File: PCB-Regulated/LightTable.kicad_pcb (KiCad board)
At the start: 2 copper layers, 22 parts, among them CON1 BARREL_JACK, P1 CONN_2_V, P2 CONN_01X01, P3 CONN_01X01, P4 CONN_01X01, P5 CONN_01X01, P6 CONN_01X01, P7 CONN_01X01, P8 CONN_4_V, U1 MosfetIRF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

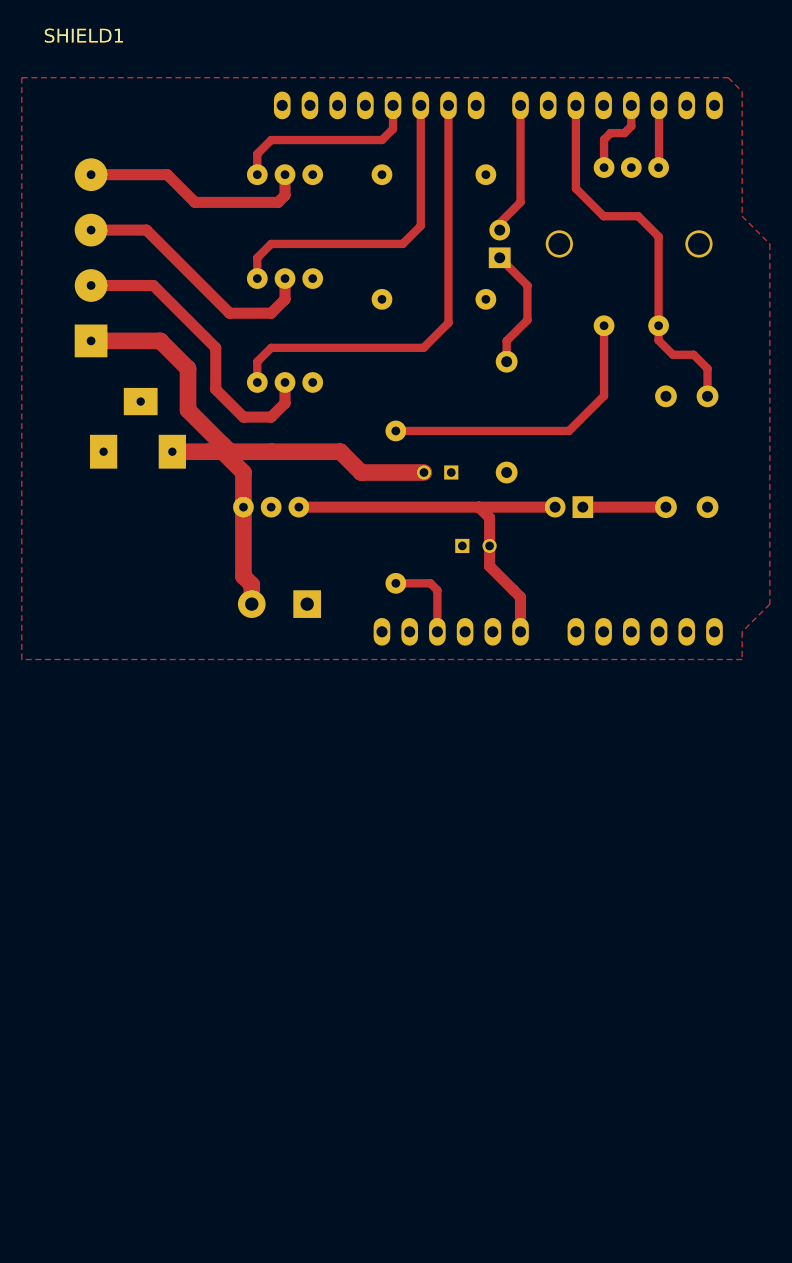
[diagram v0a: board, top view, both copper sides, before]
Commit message: Fixed wrong placement of shield
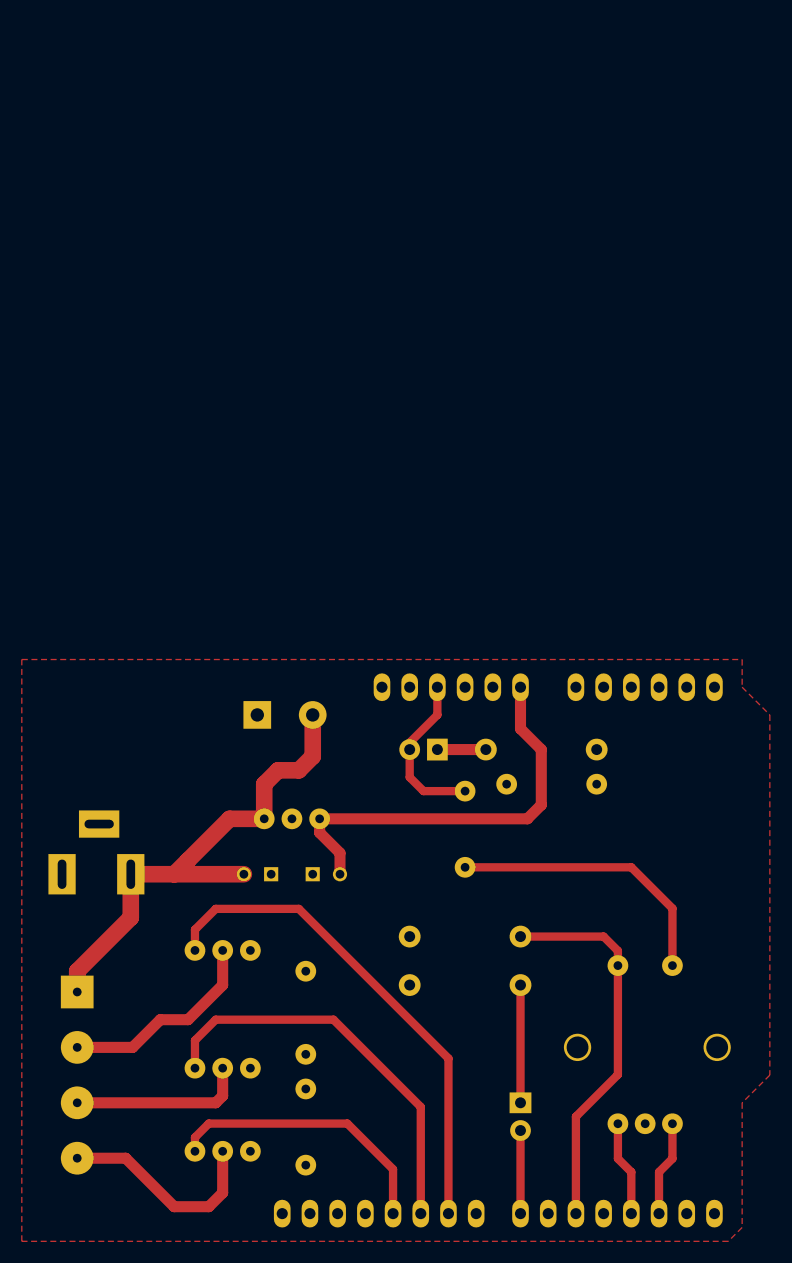
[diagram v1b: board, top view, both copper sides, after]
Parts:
- added P10: CONN_01X01, library:header1x01, B.Cu at (116.8, 115.6)
- added P9: CONN_01X01, library:header1x01, B.Cu at (125.1, 115.6)
- SHIELD1: moved to B.Cu
- moved P3 92.3 mm to (98.4, 150.5)
- moved U1 89.7 mm to (88.3, 149.2)
- moved P2 84.1 mm to (98.4, 143.5)
- moved D2 77.5 mm to (118.1, 144.8), turned to 270 degrees
- moved P8 74.9 mm to (77.5, 142.2)
- moved EN1 73.7 mm to (129.5, 139.7), turned to 90 degrees
- moved U2 72.6 mm to (88.3, 141.6)
- moved P4 69.6 mm to (98.4, 140.3)
- moved P7 63.8 mm to (98.4, 132.7)
- moved U3 52.4 mm to (88.3, 130.8)
- moved R3 52.2 mm to (113.0, 134.0), turned to 180 degrees
- moved R1 49.7 mm to (113.0, 129.5), turned to 180 degrees
- moved P5 40.5 mm to (113.0, 123.2)
- moved C1 40.4 mm to (95.2, 123.8)
- moved CON1 38.9 mm to (68.6, 123.8)
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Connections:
- D1 pad 2: V5 -> VCC
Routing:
- net +12V: track 59.6 -> 46.0 mm
- net B: track 27.4 -> 18.9 mm
- net PWM_R: track 17.5 -> 25.8 mm
- net PWM_G: track 29.1 -> 37.1 mm
- net G: track 23.4 -> 16.1 mm
- net VCC: track 34.7 -> 41.4 mm
- net PWM_B: track 40.8 -> 45.8 mm
- net Net-(D2-Pad2): track 12.2 -> 7.62 mm
- net Net-(D1-Pad1): track 7.62 -> 4.45 mm
- net Net-(EN1-Pad3): track 5.72 -> 8.75 mm
- net V5: track 36.5 -> 38.3 mm
- net R: track 21.0 -> 19.5 mm
- net Net-(EN1-Pad1): track 7.48 -> 8.75 mm
- net Net-(D2-Pad1): track 11.4 -> 10.8 mm
- net PBtn: track 34.6 -> 35.2 mm

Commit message: improved pads
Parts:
- moved R3 1.91 mm to (113.0, 132.1)
- moved R1 1.27 mm to (113.0, 128.3)
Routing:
- net Net-(D2-Pad1): track 10.8 -> 12.7 mm
- net PBtn: track 35.2 -> 36.4 mm
